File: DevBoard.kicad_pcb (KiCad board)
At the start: 2 copper layers, 100 x 100 mm, 140 parts, among them J1 Audio_In, J10 Jumper, J11 RJ45, J12 Jumper, J13 Jumper, J14 Jumper, J15 Jumper, J16 Jumper, J17 Jumper, J18 DAC_I2S, J19 DAC_OUT, J2 Audio_In, J20 DAC_Amplified, J21 DAC_Amplified, J22 Voltmeter_Power, J23 Voltmeter_Positive, J24 Voltmeter_Ground, J25 Conn_01x05_Pin, J26 Pot1, J27 Pot2, J28 Pot3, J29 Pot4, J3 Audio_Amplified, J30 CV_Scaled_Out1, J31 Audio12V_In, J32 Audio_Scaled_Out, J33 CV_In2, J34 Power, J35 Power, J36 Power, J37 Power, J38 Power, J39 Power_Test, J4 Audio_Amplified, J40 Power, J41 Power_Test, J42 Power, J43 Power, J44 Pot1, J45 Pot2, J46 Pot3, J47 Pot4, J48 CV_In1, J49 CV_Scaled_Out2, J5 CV_In, J50 Audio12V_In, J51 Audio_Scaled_Out, J6 CV_Out, J7 CV_Amplified, J8 CV_Amplified, J9 Jumper, SW2 SW_DPDT_x2, U1 MCP6004, U2 TL074, U3 LM1117-3.3, U4 LM1117-5.0, U5 LM4040DBZ-5, U6 PCM5100APW, U8 TL072

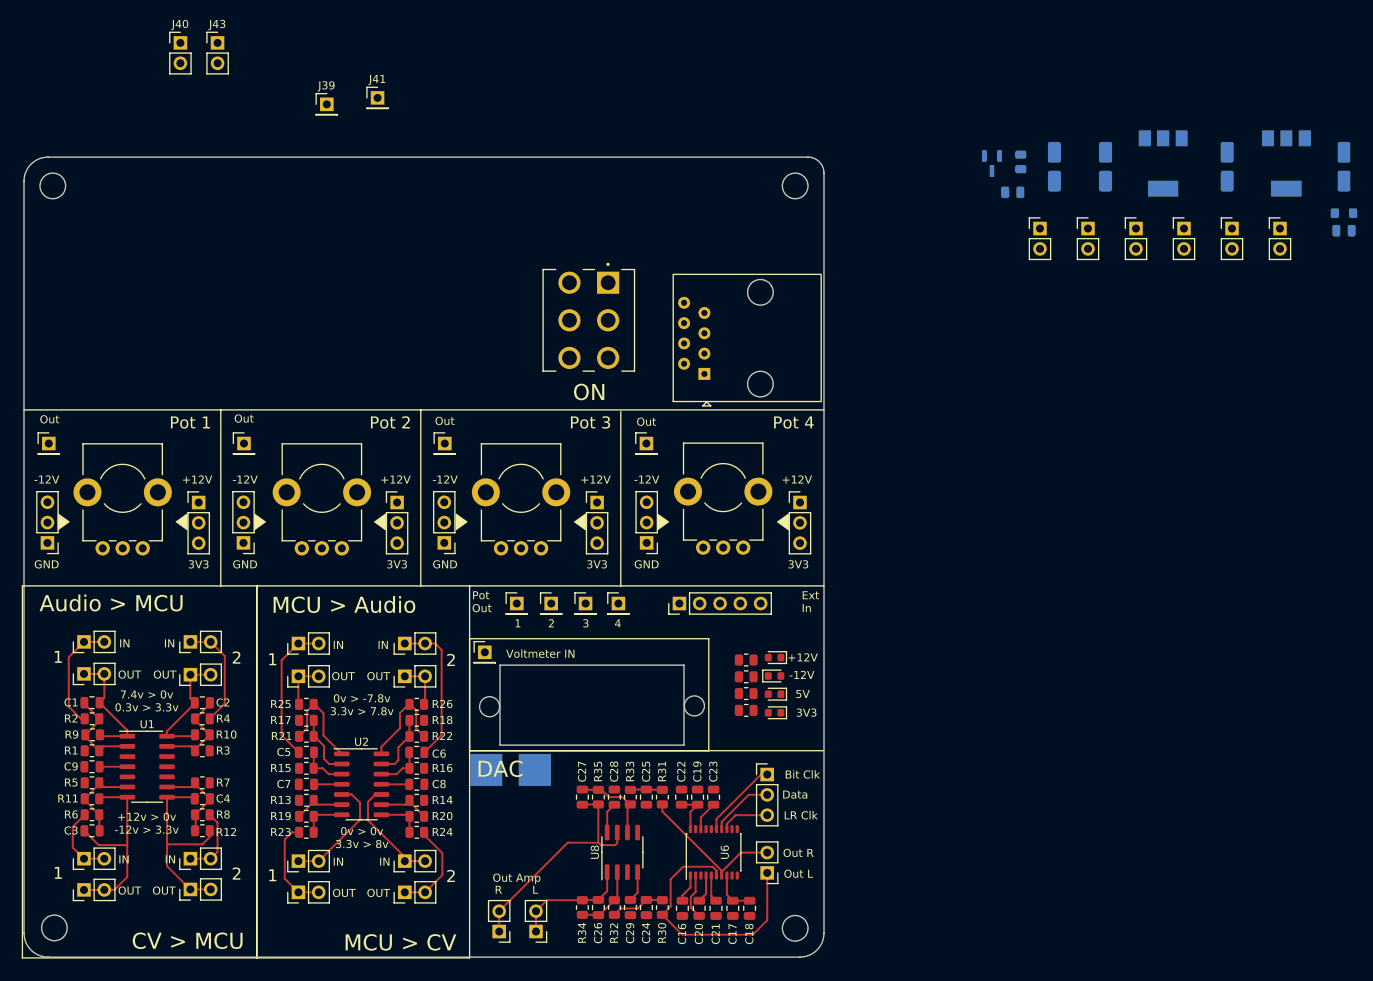
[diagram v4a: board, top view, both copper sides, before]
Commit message: First draft routing completed
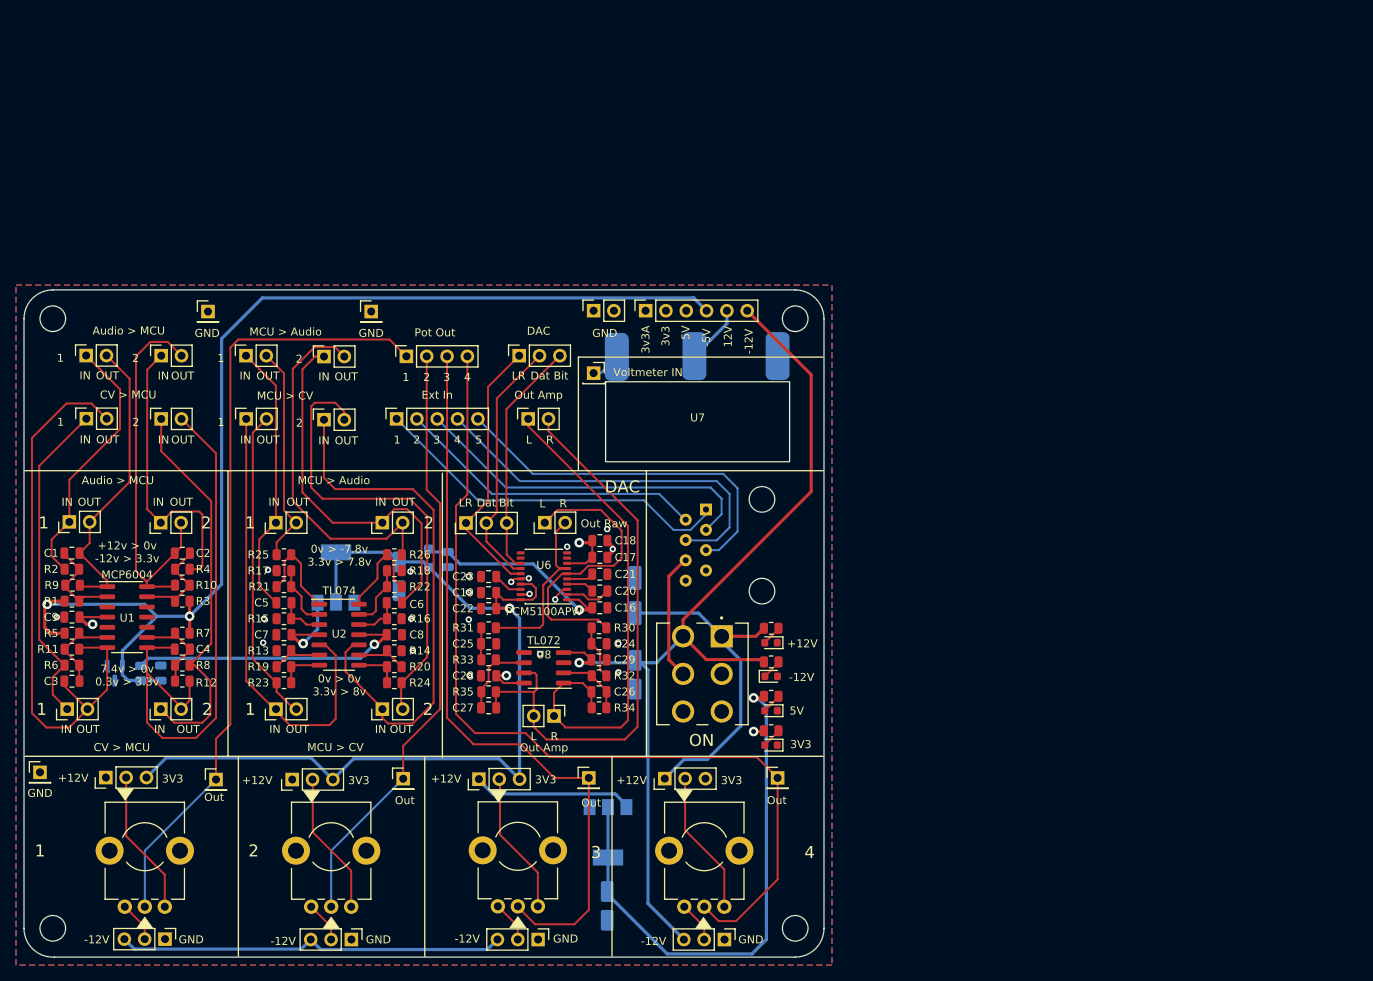
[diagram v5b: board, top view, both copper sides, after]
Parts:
- removed J24: Voltmeter_Ground, TestPoint:TestPoint_Pad_4.0x4.0mm
- removed J27: Pot2, Connector_PinHeader_2.54mm:PinHeader_1x01_P2.54mm_Vertical
- removed J28: Pot3, Connector_PinHeader_2.54mm:PinHeader_1x01_P2.54mm_Vertical
- removed J29: Pot4, Connector_PinHeader_2.54mm:PinHeader_1x01_P2.54mm_Vertical
- removed J34, J36, J37, J38, J42, J43: Power, Connector_PinHeader_2.54mm:PinHeader_1x02_P2.54mm_Vertical
- removed REF** (x2): MountingHole_2.5mm, MountingHole:MountingHole_2.5mm
- added J52: Conn_01x04_Pin, Connector_PinSocket_2.54mm:PinSocket_1x04_P2.54mm_Vertical, F.Cu at (97.8, 74.9)
- added U7: ~, Custom_Footprints:MiniVoltmeter, F.Cu at (134.2, 83.1)
- C30: footprint Capacitor_SMD:CP_Elec_4x5.8 -> Capacitor_SMD:CP_Elec_5x5.4
- J1, J20, J3, J30, J40, J49, J51, J6, J8: footprint Connector_PinHeader_2.54mm:PinHeader_1x02_P2.54mm_Vertical -> Connector_PinSocket_2.54mm:PinSocket_1x02_P2.54mm_Vertical
- J11: moved to B.Cu
- J22: value Voltmeter_Power -> Voltmeter; footprint TestPoint:TestPoint_Pad_4.0x4.0mm -> Connector_PinSocket_2.54mm:PinSocket_1x01_P2.54mm_Vertical; moved to F.Cu
- J23: value Voltmeter_Positive -> Power_Test
- J25: footprint Connector_PinHeader_2.54mm:PinHeader_1x05_P2.54mm_Vertical -> Connector_PinSocket_2.54mm:PinSocket_1x05_P2.54mm_Vertical
- J26: value Pot1 -> DAC_I2S; footprint Connector_PinHeader_2.54mm:PinHeader_1x01_P2.54mm_Vertical -> Connector_PinSocket_2.54mm:PinSocket_1x03_P2.54mm_Vertical
- J31: value Audio12V_In -> AudioToMCU; footprint Connector_PinHeader_2.54mm:PinHeader_1x02_P2.54mm_Vertical -> Connector_PinSocket_2.54mm:PinSocket_1x02_P2.54mm_Vertical
- J35: value Power -> Conn_01x06_Socket; footprint Connector_PinHeader_2.54mm:PinHeader_1x02_P2.54mm_Vertical -> Connector_PinSocket_2.54mm:PinSocket_1x06_P2.54mm_Vertical
- J50: value Audio12V_In -> AudioToMCU
- moved U3 129.6 mm to (89.0, 102.5), turned to 90 degrees
- moved C11 128.7 mm to (96.9, 102.4), turned to -90 degrees
- moved R29 127.2 mm to (64.6, 114.5)
- moved U5 126.8 mm to (61.4, 114.5)
- moved C14 122.3 mm to (67.1, 114.5), turned to 90 degrees
- moved L1 122.2 mm to (100.6, 100.1), turned to 90 degrees
- moved C13 119.3 mm to (103.0, 100.3), turned to -90 degrees
- moved C12 111.4 mm to (122.9, 143.6), turned to -90 degrees
- moved U4 108.7 mm to (123.0, 134.4)
- moved J41 94.3 mm to (52.0, 126.9)
- moved C30 91.4 mm to (126.4, 104.8), turned to 90 degrees
- moved C31 82.3 mm to (126.4, 114.7)
- moved J20 64.1 mm to (113.0, 82.7), turned to 90 degrees
- moved J40 61.5 mm to (121.2, 69.2), turned to 90 degrees
- moved J8 59.9 mm to (87.5, 82.8)
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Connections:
- net Net-(J27-Pin_1) renamed /Pot2
- net Net-(J28-Pin_1) renamed /Pot3
- net Net-(J29-Pin_1) renamed /Pot4
- C1 pad 1: /Audio_Scaled1 -> /Audio_Scaled_Out1
- C2 pad 1: /Audio_Scaled2 -> /Audio_Scaled_Out2
- J1 pad 2: /Audio_In1 -> /Audio_Out1
- J2 pad 1: /Audio_Out1 -> /Audio_In1
- J20 pad 2: /DAC_OUT_AMP_L -> /DAC_OUT_AMP_R
- J21 pad 1: /DAC_OUT_AMP_R -> /DAC_OUT_AMP_L
- J22 pad 1: +12V -> /Voltmeter_In
- J23 pad 1: +VDC -> GND
- J26 pad 1: Net-(J26-Pin_1) -> /DAC_LRCLK
- J3 pad 2: /Audio_In2 -> /Audio_Out2
- J30 pad 1: /CV_Scaled_Out1 -> /CV_In1
- J31 pad 2: /Audio12V_In1 -> /Audio_Scaled_Out1
- J32 pad 1: /Audio_Scaled2 -> /Audio12V_In2
- J32 pad 2: /Audio_Scaled2 -> /Audio_Scaled_Out2
- J33 pad 2: /CV_In2 -> /CV_Scaled_Out2
- J35 pad 1: +5V -> +3V3
- J35 pad 2: +5V -> +3.3VA
- J4 pad 1: /Audio_Out2 -> /Audio_In2
- J44 pad 1: Net-(J26-Pin_1) -> /Pot1
- J48 pad 2: /CV_In1 -> /CV_Scaled_Out1
- J49 pad 1: /CV_Scaled_Out2 -> /CV_In2
- J5 pad 2: /CV1_In -> /CV1_Out
- J50 pad 1: /Audio_Scaled1 -> /Audio12V_In1
- J50 pad 2: /Audio_Scaled1 -> /Audio_Scaled_Out1
- J51 pad 2: /Audio12V_In2 -> /Audio_Scaled_Out2
- J6 pad 1: /CV1_Out -> /CV1_In
- J7 pad 2: /CV2_In -> /CV2_Out
- J8 pad 1: /CV2_Out -> /CV2_In
- R10 pad 1: /Audio_Scaled2 -> /Audio_Scaled_Out2
- R9 pad 1: /Audio_Scaled1 -> /Audio_Scaled_Out1
- RV1 pad 2: Net-(J26-Pin_1) -> /Pot1
- U1 pad 1: /Audio_Scaled1 -> /Audio_Scaled_Out1
- U1 pad 14: /Audio_Scaled2 -> /Audio_Scaled_Out2
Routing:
- net -12V: track 7.32 -> 254.6 mm, vias 0 -> 2
- net +12V: track 7.32 -> 246.8 mm, vias 0 -> 2
- net +3V3: track 5.42 -> 205.3 mm, vias 0 -> 2
- net -5V: track 0.00 -> 144.5 mm, vias 0 -> 2
- net +3.3VA: track 12.5 -> 147.5 mm, vias 0 -> 3
- net +5V: track 0.00 -> 133.1 mm, vias 0 -> 1
- net /Pot4: track 0.00 -> 113.6 mm
- net /Pot1: track 0.00 -> 97.6 mm
- net /Pot3: track 0.00 -> 93.1 mm
- net /Pot2: track 0.00 -> 75.1 mm
- net /CV2_In: track 14.0 -> 66.7 mm
- net /Audio_Scaled_Out2: track 0.00 -> 49.4 mm
- net /DAC_OUT_AMP_L: track 14.9 -> 63.6 mm
- net /Interconnect4_GATE: track 0.00 -> 48.3 mm
- net /CV_Scaled_Out2: track 25.5 -> 73.5 mm
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- added copper zone on B.Cu, net GND
- added copper zone on F.Cu, net GND
- added copper zone on In1.Cu, net GND
- added copper zone on In2.Cu, net GND
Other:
- board size 100 x 100 mm -> 100 x 83.4 mm
- copper layers 2 -> 4
- board text added: "-5V"
- board text added: "12V"
- board text added: "3v3"
- board text added: "3v3A"
- board text added: "5"
- board text added: "Bit"
- board text added: "Dat"
- board text added: "LR"
- board text added: "Out Raw"
- board text removed: "Bit Clk"
- board text removed: "Data"
- board text removed: "LR Clk"
- board text removed: "Out L"
- board text removed: "Out R"
- board text removed: "Pot 1"
- board text removed: "Pot 2"
- board text removed: "Pot 3"
- board text removed: "Pot 4"

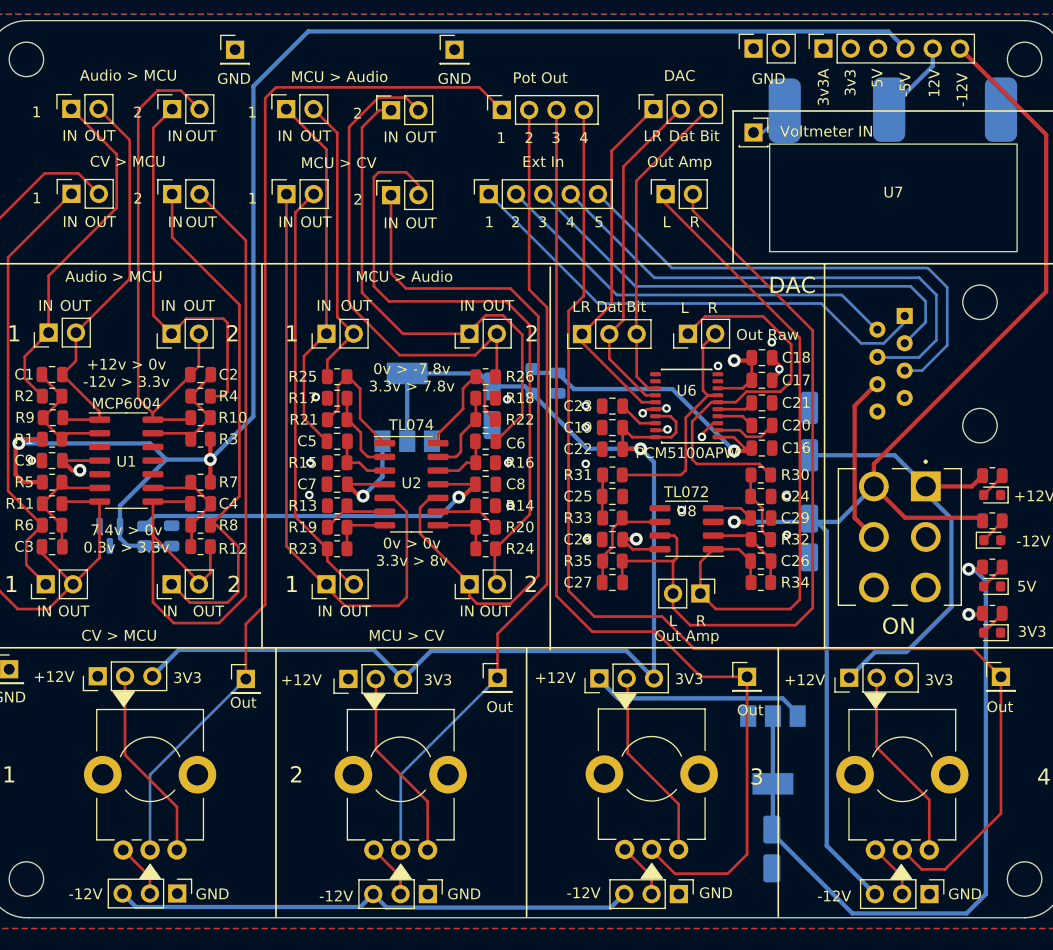
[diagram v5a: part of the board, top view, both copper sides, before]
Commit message: Cleaned up schematic
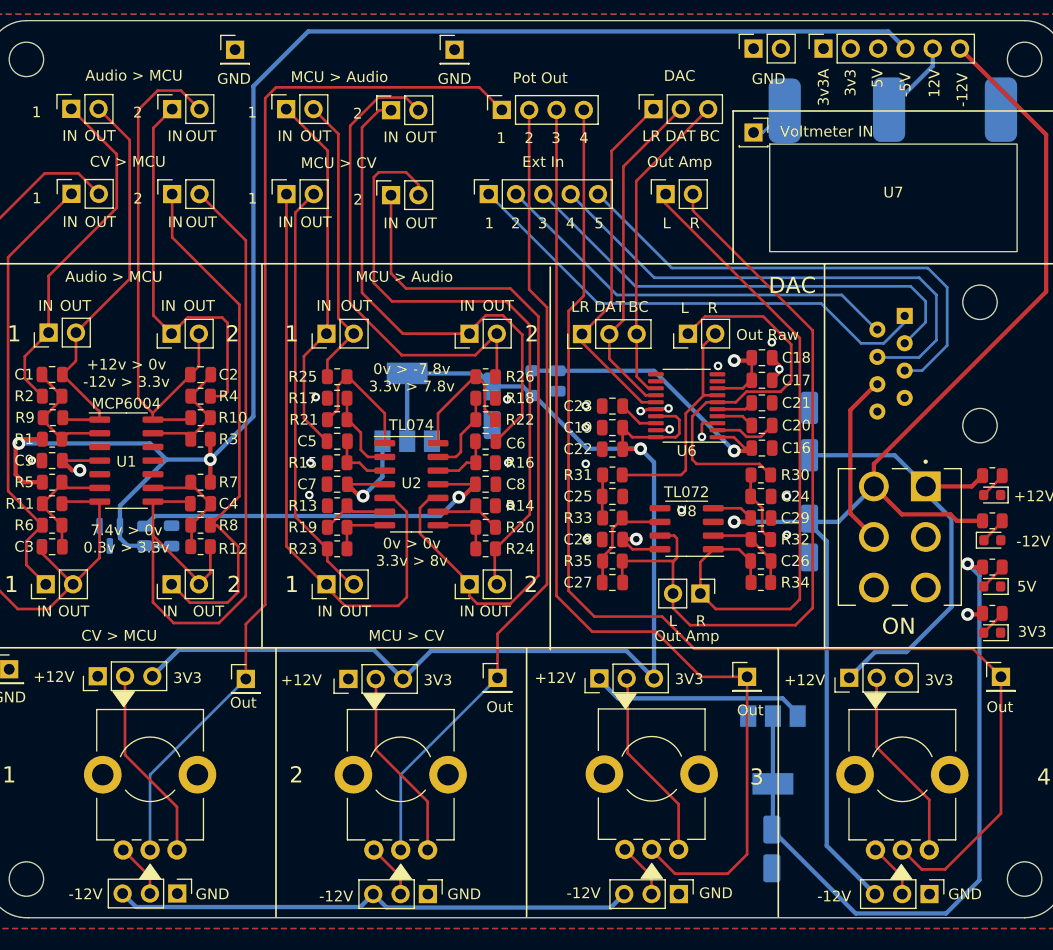
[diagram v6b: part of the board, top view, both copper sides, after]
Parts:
- J1, J2: value Audio_In -> MCUToAudio1
- J23, J39, J41: value Power_Test -> Ground
- J25: value Conn_01x05_Pin -> Interconnects
- J3, J4: value Audio_Amplified -> MCUToAudio2
- J31, J50: value AudioToMCU -> AudioToMCU1
- J32, J51: value Audio_Scaled_Out -> AudioToMCU2
- J35: value Conn_01x06_Socket -> Power
- J40: value Power -> Ground
- J5: value CV_In -> MCUToCV1
- J52: value Conn_01x04_Pin -> Pot_Out
- J6: value CV_Out -> MCUToCV1
- J7, J8: value CV_Amplified -> MCUToCV2
- U6: footprint Custom_Footprints:SSOP-20_4.4x6.5mm_Pitch0.65mm_Round_Pads -> Package_SO:TSSOP-20_4.4x6.5mm_P0.65mm
- moved C13 0.20 mm to (103.0, 100.1)
- moved L1 0.20 mm to (100.6, 100.3)
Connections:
- net +3V3 renamed +3.3V
- net /Audio12V_In1 renamed /EurorackToMCU/Audio12V_In1
- net /Audio12V_In2 renamed /EurorackToMCU/Audio12V_In2
- net /Audio_In1 renamed /MCUToEurorack/Audio_In1
- net /Audio_In2 renamed /MCUToEurorack/Audio_In2
- net /Audio_Out1 renamed /MCUToEurorack/Audio_Out1
- net /Audio_Out2 renamed /MCUToEurorack/Audio_Out2
- net /Audio_Scaled_Out1 renamed /EurorackToMCU/Audio_Scaled_Out1
- net /Audio_Scaled_Out2 renamed /EurorackToMCU/Audio_Scaled_Out2
- net /CV1_In renamed /MCUToEurorack/CV1_In
- net /CV1_Out renamed /MCUToEurorack/CV1_Out
- net /CV2_In renamed /MCUToEurorack/CV2_In
- net /CV2_Out renamed /MCUToEurorack/CV2_Out
- net /CV_In1 renamed /EurorackToMCU/CV_In1
- net /CV_In2 renamed /EurorackToMCU/CV_In2
- net /CV_Scaled_Out1 renamed /EurorackToMCU/CV_Scaled_Out1
- net /CV_Scaled_Out2 renamed /EurorackToMCU/CV_Scaled_Out2
- net /DAC_BCLK renamed /DAC/DAC_BCLK
- net /DAC_DATA renamed /DAC/DAC_DATA
- net /DAC_LRCLK renamed /DAC/DAC_LRCLK
- net /DAC_OUT_AMP_L renamed /DAC/DAC_OUT_AMP_L
- net /DAC_OUT_AMP_R renamed /DAC/DAC_OUT_AMP_R
- net /DAC_OUT_L renamed /DAC/DAC_OUT_L
- net /DAC_OUT_R renamed /DAC/DAC_OUT_R
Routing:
- net +5V: track 133.1 -> 130.8 mm
- net /DAC/DAC_OUT_R: track 22.2 -> 21.3 mm
- net +3.3V: track 205.3 -> 206.1 mm
- net GND: track 8.35 -> 8.91 mm
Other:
- board text added: "BC"
- board text added: "DAT"
- board text added: "Eurorack Dev Board v2.0 2023 Mountjoy Modular"
- board text removed: "Bit"
- board text removed: "Dat"
